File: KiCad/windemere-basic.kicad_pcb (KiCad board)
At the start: 2 copper layers, 152.4 x 158.7 mm, 61 parts, among them J1 Barrel_Jack, J2 Connector, SW1 SW_SPDT, SW2 Reset Button, U1 L7805, U2 74HC00, U3 WD65C02, U4 28C256, U5 62256, U6 WD65C22, U7 MM74C922, U8 HD44780U, U9 MCP102-475, X1 1MHz

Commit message: update to current
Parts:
- removed SW1: SW_SPDT, Button_Switch_THT:SW_E-Switch_EG1271_DPDT
- SW2: footprint footprints:D6R90F1LFS -> Button_Switch_THT:SW_PUSH_6mm
- moved memory_map 26.7 mm to (260.9, 55.6)
- moved D1 10.2 mm to (178.4, 49.1), turned to 180 degrees
- moved C6 4.91 mm to (173.7, 181.6), turned to -90 degrees
- moved C1 0.73 mm to (153.9, 61.6)
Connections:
- J1 pad 1: Net-(J1-Pad1) -> Net-(D1-Pad2)
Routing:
- net +5V: track 0.00 -> 497.5 mm
- net Net-(KB1-Pad2): track 0.00 -> 200.9 mm
- net Net-(J2-Pad28): track 0.00 -> 187.6 mm, vias 0 -> 2
- net Net-(C4-Pad1): track 0.00 -> 176.8 mm
- net Net-(D3-Pad2): track 0.00 -> 174.1 mm
- net Net-(KB5-Pad2): track 0.00 -> 159.9 mm
- net Net-(D5-Pad2): track 0.00 -> 159.5 mm
- net Net-(D4-Pad2): track 0.00 -> 156.3 mm
- net /D1: track 0.00 -> 148.9 mm
- net /D0: track 0.00 -> 148.8 mm
- net /D2: track 0.00 -> 148.7 mm
- net /A0: track 0.00 -> 147.7 mm
- net /D3: track 0.00 -> 145.9 mm
- net /A14: track 0.00 -> 140.6 mm
- net /D4: track 0.00 -> 140.4 mm
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- added copper zone on B.Cu, net GND

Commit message: Update ID's
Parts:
- renumbered C4 to C1, C3 to C2, C5 to C3, C6 to C4, C1 to C5, C2 to C6, D2 to D1, D1 to D2, J2 to J1, J1 to J2, KB18 to KB10, KB3 to KB11, KB7 to KB12, KB11 to KB13, KB15 to KB14, KB19 to KB15, KB4 to KB16, KB8 to KB17, KB12 to KB18, KB16 to KB19, KB5 to KB2, KB9 to KB3, KB13 to KB4, KB17 to KB5, KB2 to KB6, KB6 to KB7, KB10 to KB8, KB14 to KB9, R8 to R1, R1 to R2, R2 to R3, R3 to R4, R4 to R5, R5 to R6, R6 to R7, R7 to R8, SW2 to SW1, U8 to U1, U3 to U2, U4 to U3, U5 to U4, U6 to U5, U2 to U6, U1 to U8

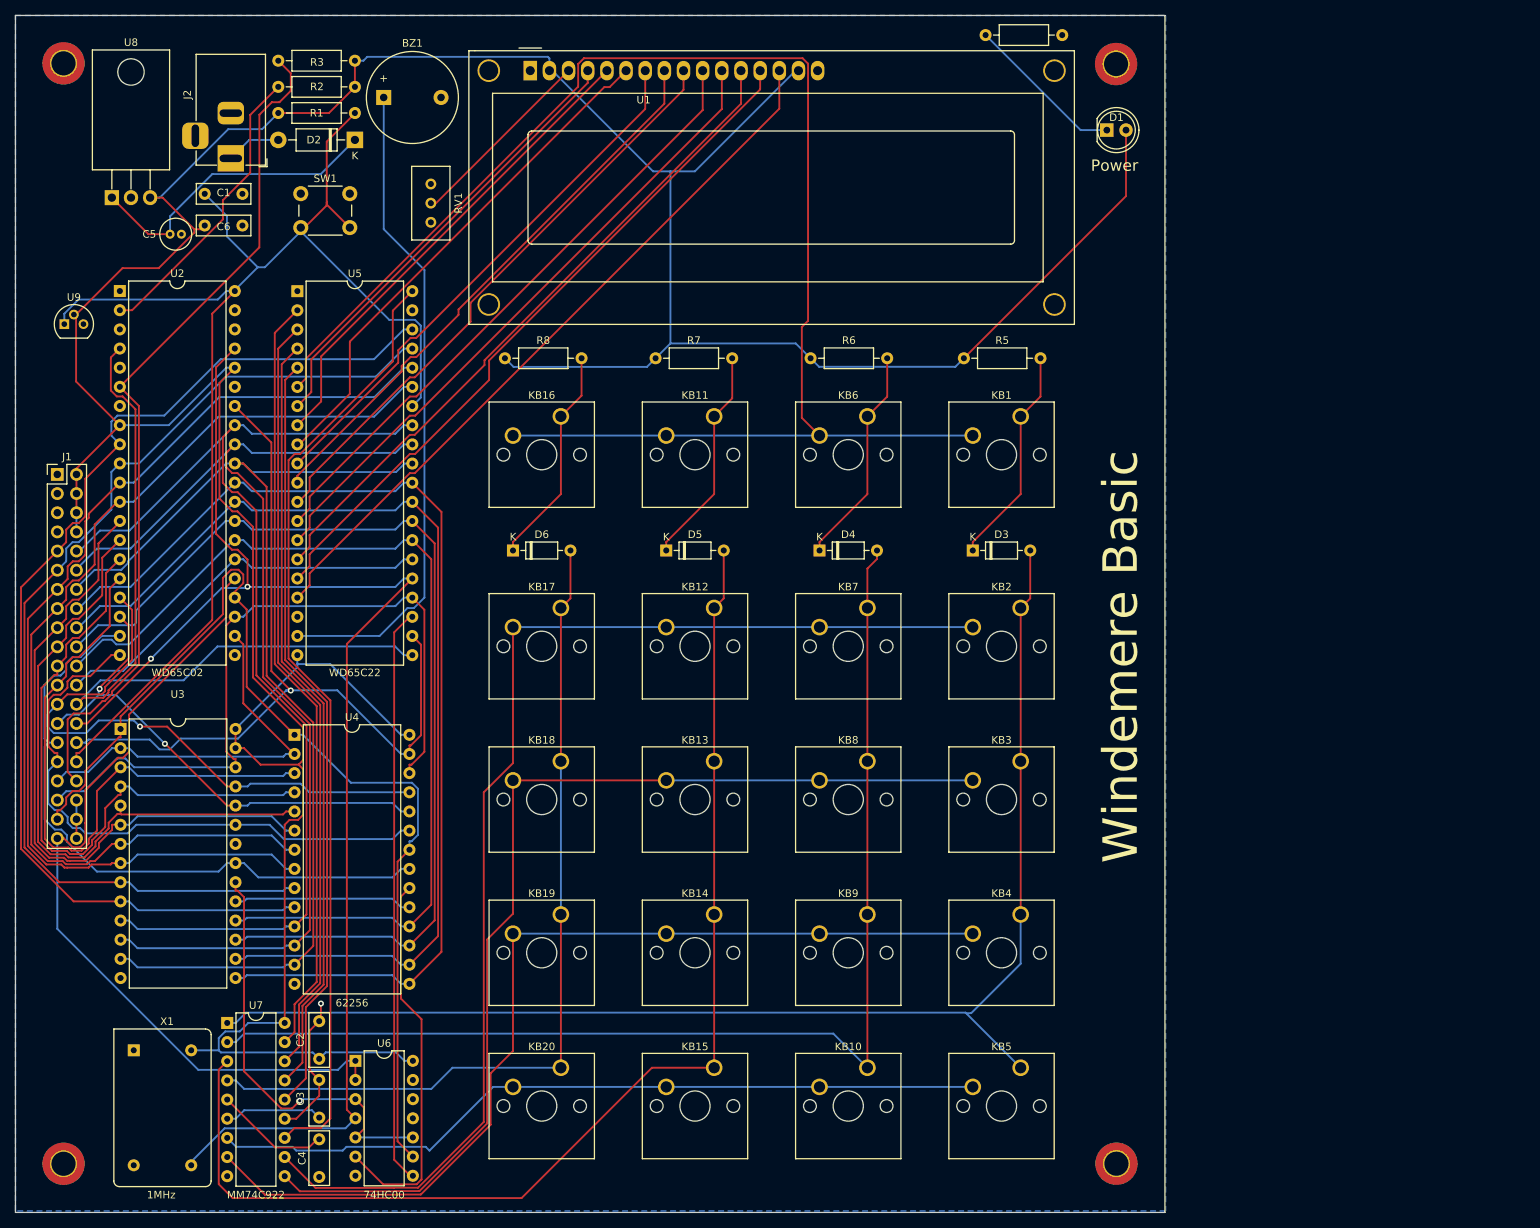
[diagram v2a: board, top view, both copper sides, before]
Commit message: Add Bypass caps
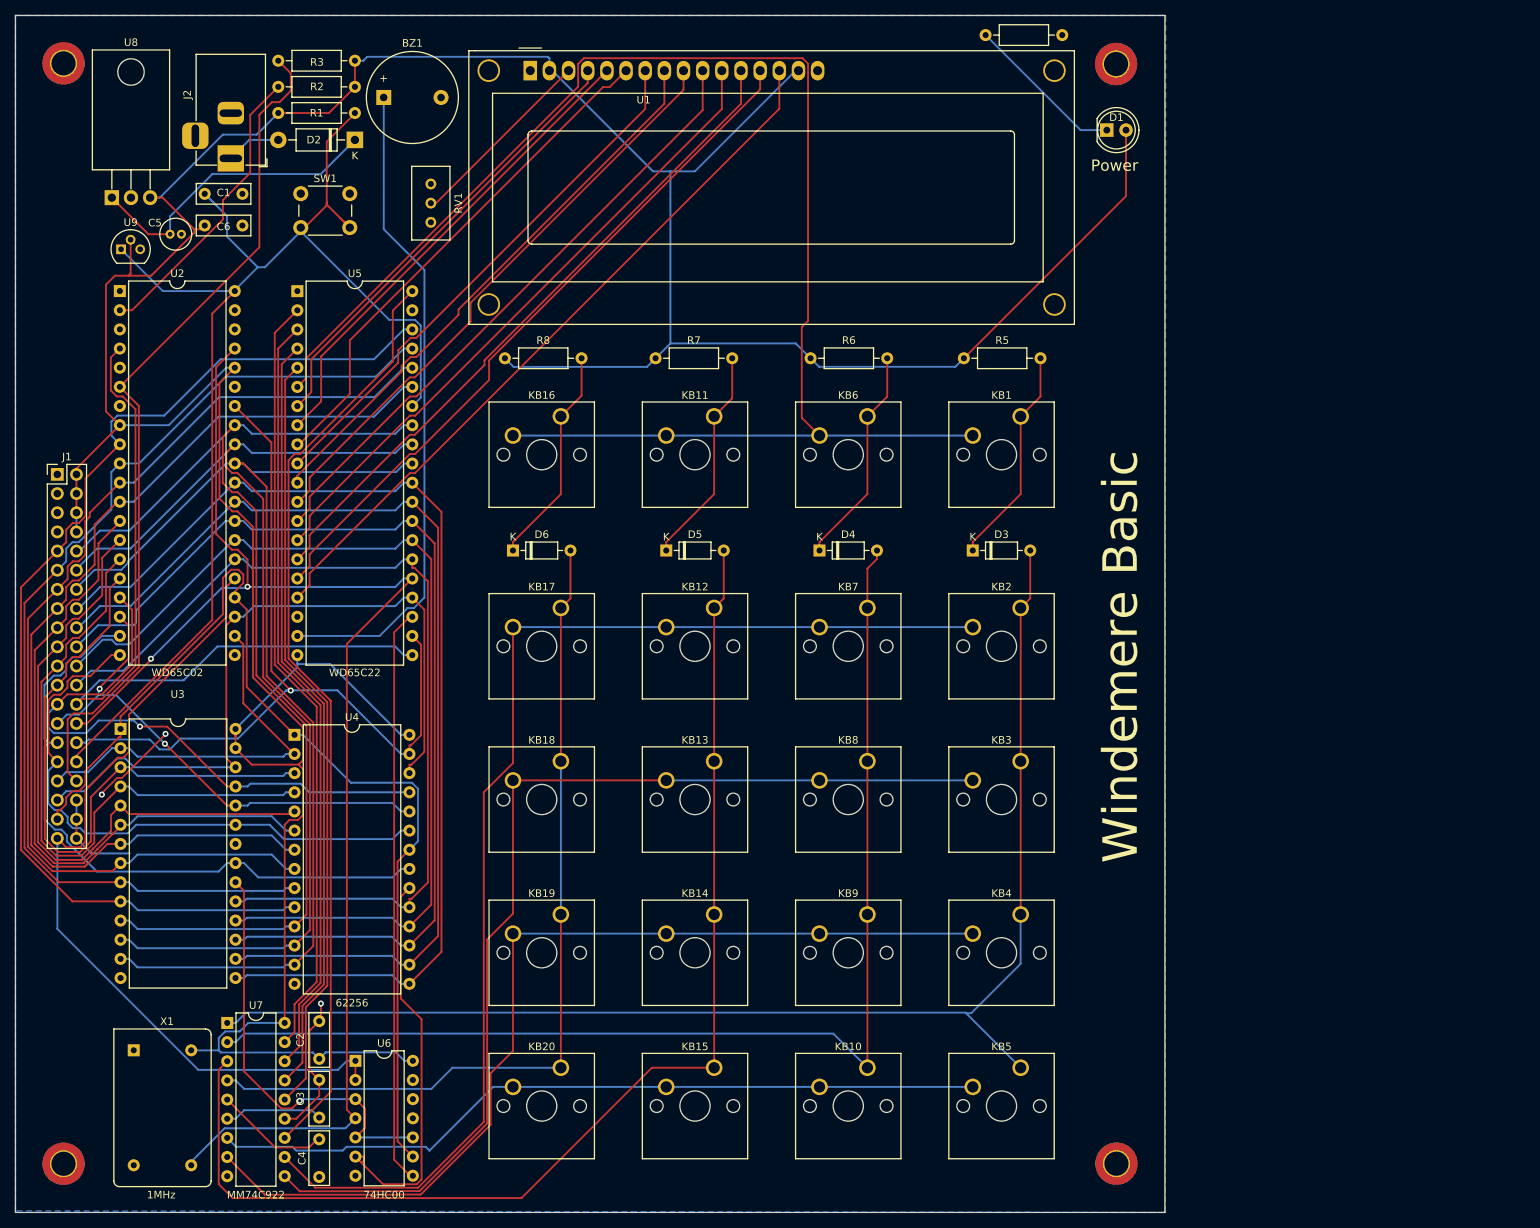
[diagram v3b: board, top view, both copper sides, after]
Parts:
- moved U9 12.5 mm to (147.4, 63.6)
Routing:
- net /D7: track 76.1 -> 124.4 mm
- net GND: track 24.4 -> 44.2 mm, vias 1 -> 3
- net Net-(C1-Pad1): track 176.8 -> 172.7 mm
- net +5V: track 497.5 -> 500.4 mm
- net Net-(U4-Pad20): track 50.8 -> 52.9 mm
- net Net-(U5-Pad40): track 126.3 -> 124.3 mm
- net Net-(U3-Pad20): track 56.7 -> 58.2 mm

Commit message: updates
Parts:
- added C1: 0.1uF, Capacitor_THT:C_Disc_D7.0mm_W2.5mm_P5.00mm, F.Cu at (141.6, 83.4)
- added C10: 0.1uF, Capacitor_THT:C_Disc_D7.0mm_W2.5mm_P5.00mm, F.Cu at (175.0, 120.5)
- added C11: 0.1uF, Capacitor_THT:C_Disc_D7.0mm_W2.5mm_P5.00mm, F.Cu at (327.3, 75.0)
- added C4: 0.1uF, Capacitor_THT:C_Disc_D7.0mm_W2.5mm_P5.00mm, F.Cu at (166.6, 129.3)
- added C5: 0.1uF, Capacitor_THT:C_Disc_D7.0mm_W2.5mm_P5.00mm, F.Cu at (327.3, 71.0)
- renumbered C5 to C2, C6 to C3, C2 to C6, C1 to C7, C3 to C8, C4 to C9, D2 to D1, D1 to D2, J2 to J1, J1 to J2, KB8 to KB10, KB13 to KB11, KB18 to KB12, KB4 to KB13, KB9 to KB14, KB14 to KB15, KB19 to KB16, KB5 to KB17, KB10 to KB18, KB15 to KB19, KB6 to KB2, KB11 to KB3, KB16 to KB4, KB2 to KB5, KB7 to KB6, KB12 to KB7, KB17 to KB8, KB3 to KB9, R2 to R1, R3 to R2, R4 to R3, R5 to R4, R6 to R5, R7 to R6, R8 to R7, R1 to R8, U8 to U1, U6 to U2, U2 to U3, U3 to U4, U4 to U5, U5 to U6, U1 to U8
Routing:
- net +5V: track 500.4 -> 516.3 mm
- net Net-(J2-Pad30): track 109.9 -> 111.8 mm
- net /D2: track 148.7 -> 148.1 mm

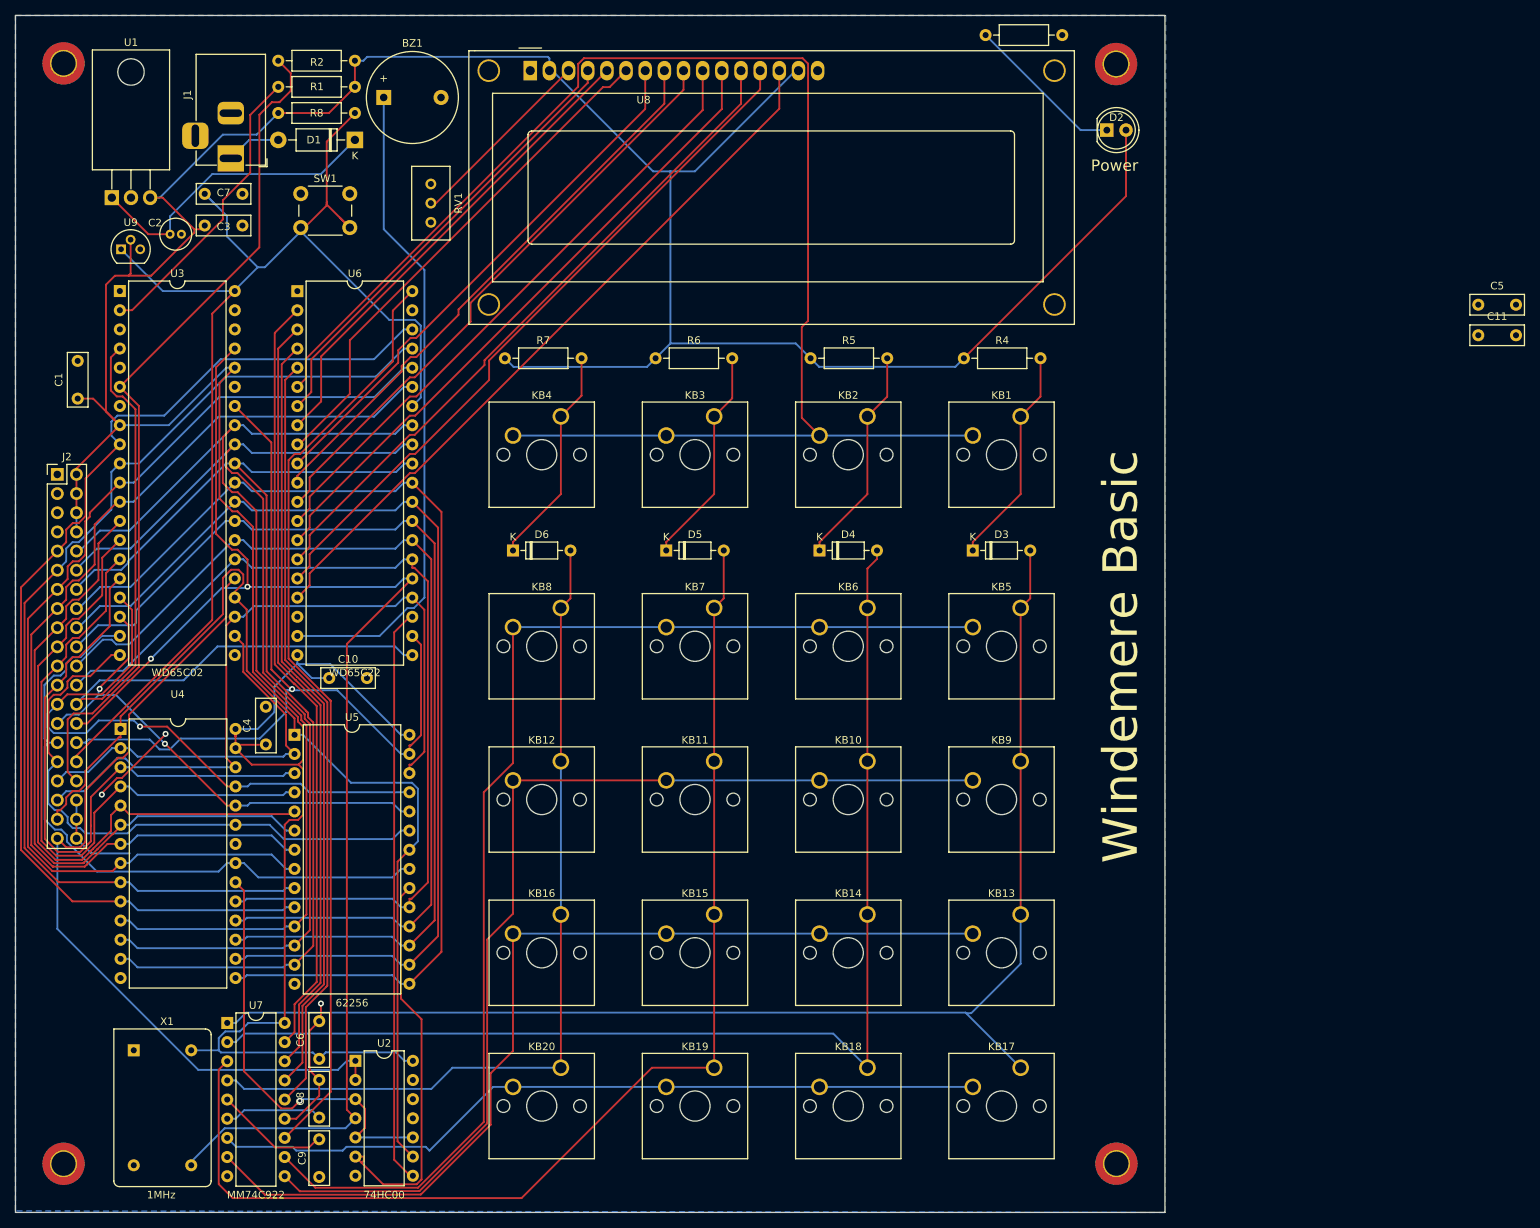
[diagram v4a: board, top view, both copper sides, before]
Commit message: minor footprint changes.
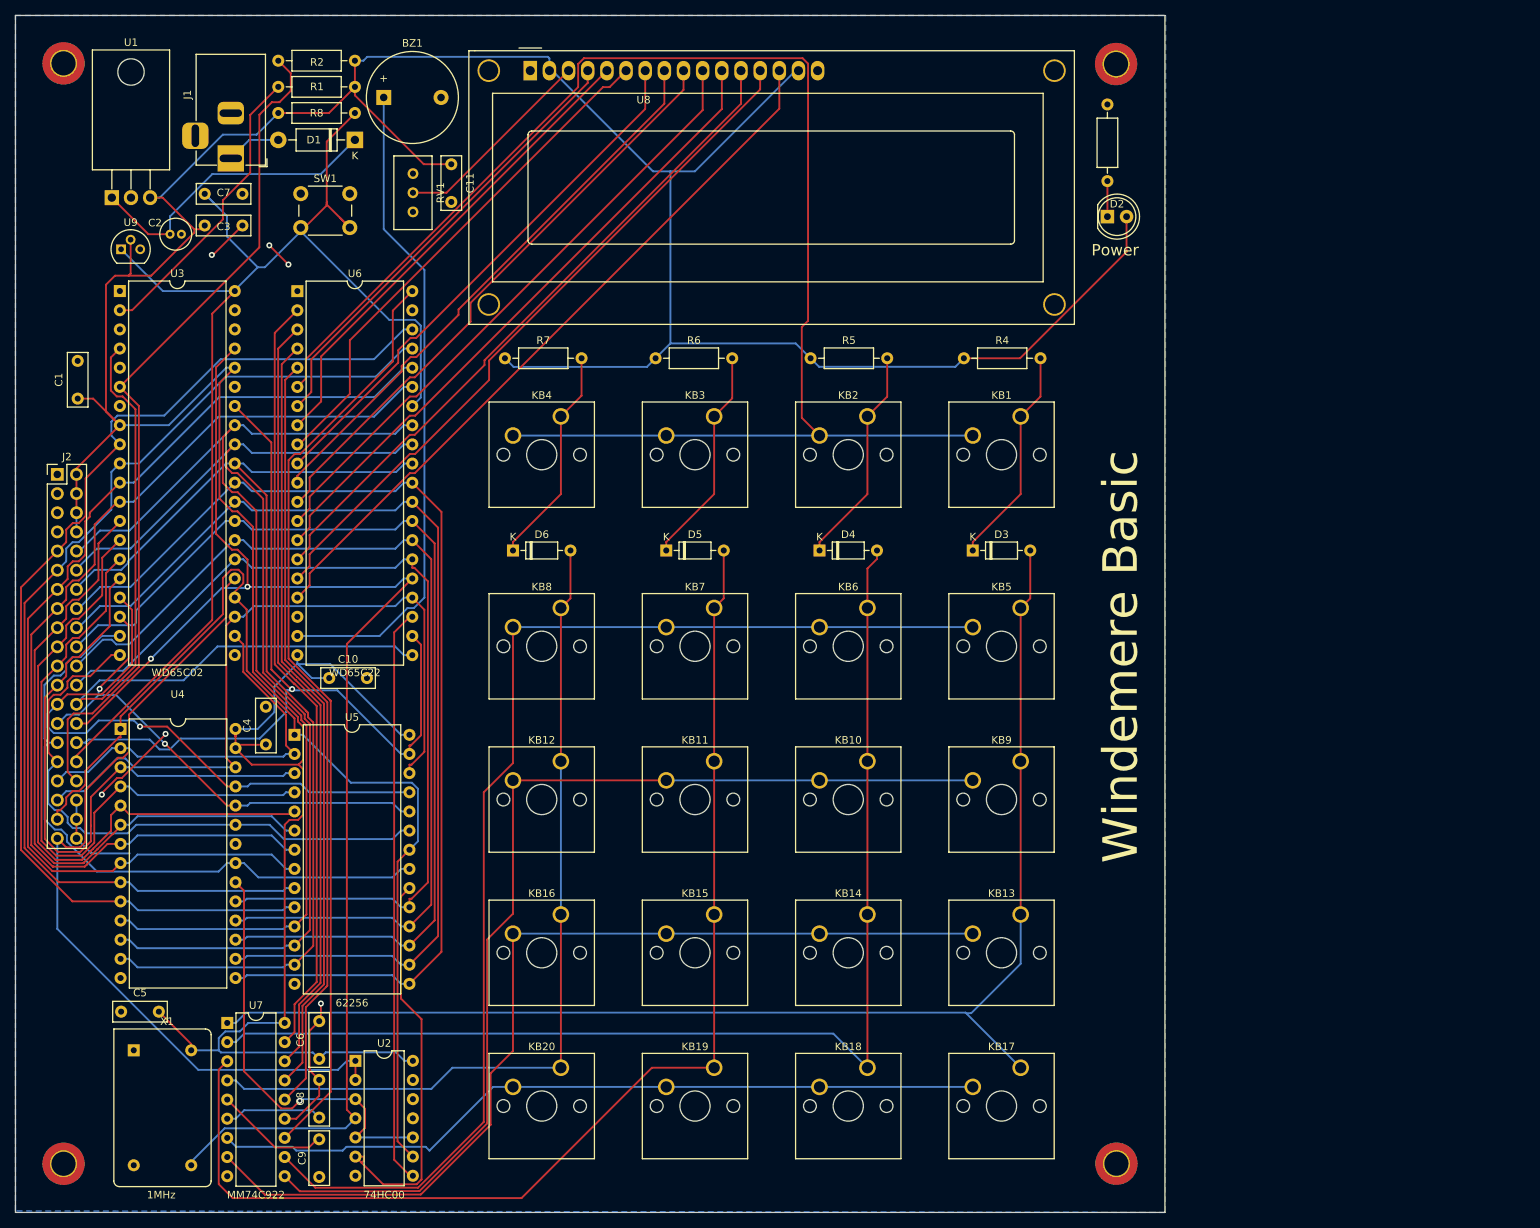
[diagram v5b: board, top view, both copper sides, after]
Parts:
- moved C5 198.5 mm to (152.4, 164.7), turned to 180 degrees
- moved C11 138.0 mm to (191.2, 52.4), turned to -90 degrees
- moved R3 25.2 mm to (278.1, 54.6), turned to 90 degrees
- moved D2 11.5 mm to (278.1, 59.3)
- moved RV1 2.74 mm to (186.1, 58.7)
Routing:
- net +5V: track 516.3 -> 533.8 mm
- net Net-(D2-Pad1): track 21.3 -> 4.71 mm
- net GND: track 44.2 -> 53.4 mm, vias 3 -> 6
- net Net-(RV1-Pad2): track 25.5 -> 27.3 mm
